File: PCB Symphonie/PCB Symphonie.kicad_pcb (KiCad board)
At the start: 2 copper layers, 81 parts, among them J1 Neopixel Clavier, J2 Neopixel Indicateur batterie, J3 Bornier Alim Ampli, J4 Bornier Signal ampli, Q1 2N3905, Q2 2N3905, Q3 2N3905, Q4 2N3905, SW0 SW_Push, SW1 SW_Push, SW10 SW_Push, SW11 SW_Push, SW12 SW_Push, SW13 SW_Push, SW14 SW_Push, SW15 SW_Push, SW16 SW_Push, SW17 SW_Push, SW18 SW_Push, SW19 SW_Push, SW2 SW_Push, SW20 SW_Push, SW21 SW_Push, SW22 SW_Push, SW23 SW_Push, SW24 SW_Push, SW3 SW_Push, SW4 SW_Push, SW5 SW_Push, SW6 SW_Push, SW7 SW_Push, SW8 SW_Push, SW9 SW_Push, U1 LM317_TO-220, U2 LM317_TO-220, U3 LM317_TO-220, U4 LM317_TO-220

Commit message: MAJ Pin changement shematique verifier empreintes
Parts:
- removed D15, D16, D17, D18, D19, D20, D21, D22, D23, D24: 1N4148, Diode_THT:D_DO-35_SOD27_P7.62mm_Horizontal
- removed SW0, SW1, SW10, SW11, SW12, SW13, SW14, SW15, SW16, SW17, SW18, SW19, SW2, SW20, SW21, SW22, SW23, SW24, SW3, SW4, SW5, SW6, SW7, SW8, SW9: SW_Push, Button_Switch_THT:SW_Tactile_Straight_KSA0Axx1LFTR
- added C1: C_Polarized_Small, Capacitor_SMD:CP_Elec_5x5.4, F.Cu at (89.5, 40.6)
- added C10: C, Capacitor_THT:CP_Radial_D8.0mm_P3.80mm, F.Cu at (76.8, 22.9)
- added C11: C, Capacitor_THT:CP_Radial_D8.0mm_P3.80mm, F.Cu at (76.8, 32.4)
- added C12: C_Polarized_Small, Capacitor_SMD:CP_Elec_5x5.4, F.Cu at (89.5, 61.2)
- added C2: C, Capacitor_THT:CP_Radial_D8.0mm_P3.80mm, F.Cu at (47.5, 22.9)
- added C3: C, Capacitor_THT:CP_Radial_D8.0mm_P3.80mm, F.Cu at (47.5, 32.4)
- added C4: C, Capacitor_THT:CP_Radial_D8.0mm_P3.80mm, F.Cu at (57.3, 22.9)
- added C5: C, Capacitor_THT:CP_Radial_D8.0mm_P3.80mm, F.Cu at (57.3, 32.4)
- added C6: C_Polarized_Small, Capacitor_SMD:CP_Elec_5x5.4, F.Cu at (89.5, 47.5)
- added C7: C, Capacitor_THT:CP_Radial_D8.0mm_P3.80mm, F.Cu at (67.0, 22.9)
- added C8: C, Capacitor_THT:CP_Radial_D8.0mm_P3.80mm, F.Cu at (67.0, 32.4)
- added C9: C_Polarized_Small, Capacitor_SMD:CP_Elec_5x5.4, F.Cu at (89.5, 54.3)
- added D25: LED, LED_THT:LED_D3.0mm, F.Cu at (91.3, 78.7)
- added D26: LED, LED_THT:LED_D3.0mm, F.Cu at (91.3, 84.2)
- added D27: LED, LED_THT:LED_D3.0mm, F.Cu at (91.3, 89.7)
- added J10: Bornier alim neopix, Connector:JWT_A3963_1x02_P3.96mm_Vertical, F.Cu at (68.9, 89.5)
- added J5: Conn_01x15_Pin, Connector_PinHeader_2.54mm:PinHeader_1x15_P2.54mm_Vertical, F.Cu at (78.0, 39.5)
- added J6: Conn_01x15_Pin, Connector_PinHeader_2.54mm:PinHeader_1x15_P2.54mm_Vertical, F.Cu at (82.7, 39.5)
- added J7: Conn_01x12_Pin, Connector_PinSocket_2.54mm:PinSocket_1x12_P2.54mm_Vertical, F.Cu at (87.3, 66.9)
- added J9: Bornier alim neopix, Connector:JWT_A3963_1x02_P3.96mm_Vertical, F.Cu at (68.9, 79.9)
- added R18: R, Resistor_THT:R_Axial_DIN0204_L3.6mm_D1.6mm_P7.62mm_Horizontal, F.Cu at (45.9, 92.3)
- added R19: R, Resistor_THT:R_Axial_DIN0204_L3.6mm_D1.6mm_P7.62mm_Horizontal, F.Cu at (45.9, 95.5)
- added SW25: SW_Push_Open, Connector_USB:USB_C_Plug_JAE_DX07P024AJ1, F.Cu at (99.1, 40.1)
- J1: value Neopixel Clavier -> Neopix batt; footprint Connector_PinHeader_2.54mm:PinHeader_1x04_P2.54mm_Vertical -> Connector:JWT_A3963_1x02_P3.96mm_Vertical
- J2: value Neopixel Indicateur batterie -> Neopix piano; footprint Connector_PinHeader_2.54mm:PinHeader_1x04_P2.54mm_Vertical -> Connector:JWT_A3963_1x02_P3.96mm_Vertical
- Q1, Q2, Q3, Q4: footprint Package_TO_SOT_THT:TO-3P-3_Horizontal_TabDown -> Package_TO_SOT_THT:TO-3P-3_Vertical
- RV1: footprint Potentiometer_SMD:Potentiometer_ACP_CA6-VSMD_Vertical -> Potentiometer_THT:Potentiometer_ACP_CA9-H5_Horizontal
- U1, U2, U3, U4: footprint Package_TO_SOT_SMD:SOT-89-3_Handsoldering -> Package_TO_SOT_THT:TO-3P-3_Vertical
- moved U1 68.1 mm to (30.5, 49.1)
- moved U2 68.0 mm to (30.5, 55.9)
- moved U3 67.8 mm to (30.5, 62.7)
- moved U4 67.7 mm to (30.5, 69.5)
- moved D28 66.3 mm to (56.6, 92.2)
- moved Q4 63.9 mm to (30.5, 42.3)
- moved D14 62.8 mm to (56.6, 88.7)
- moved D9 62.8 mm to (56.6, 70.9)
- moved D10 62.8 mm to (56.6, 74.5)
- moved D11 62.8 mm to (56.6, 78.0)
- moved D12 62.8 mm to (56.6, 81.6)
- moved D13 62.8 mm to (56.6, 85.1)
- moved Q1 62.5 mm to (30.5, 21.9)
- moved Q3 57.9 mm to (30.5, 35.5)
- moved Q2 57.4 mm to (30.5, 28.7)
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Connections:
- D0 pad 2: Net-(D0-A) -> unconnected-(D0-A-Pad2)
- D1 pad 2: Net-(D1-A) -> unconnected-(D1-A-Pad2)
- D10 pad 2: Net-(D10-A) -> unconnected-(D10-A-Pad2)
- D11 pad 2: Net-(D11-A) -> unconnected-(D11-A-Pad2)
- D12 pad 2: Net-(D12-A) -> unconnected-(D12-A-Pad2)
- D13 pad 2: Net-(D13-A) -> unconnected-(D13-A-Pad2)
- D14 pad 2: Net-(D14-A) -> unconnected-(D14-A-Pad2)
- D2 pad 2: Net-(D2-A) -> unconnected-(D2-A-Pad2)
- D3 pad 2: Net-(D3-A) -> unconnected-(D3-A-Pad2)
- D4 pad 2: Net-(D4-A) -> unconnected-(D4-A-Pad2)
- D5 pad 2: Net-(D5-A) -> unconnected-(D5-A-Pad2)
- D6 pad 2: Net-(D6-A) -> unconnected-(D6-A-Pad2)
- D7 pad 2: Net-(D7-A) -> unconnected-(D7-A-Pad2)
- D8 pad 2: Net-(D8-A) -> unconnected-(D8-A-Pad2)
- D9 pad 2: Net-(D9-A) -> unconnected-(D9-A-Pad2)
- J1 pad 1: NEOPIX 1 -> ROW0
- J1 pad 2: GND MC -> Net-(J1-Pin_2)
- J2 pad 1: NEOPIX 2 -> ROW0
- J2 pad 2: GND MC -> Net-(J2-Pin_2)
- Q3 pad 3: 5V Alim -> Net-(J9-Pin_2)
- R10 pad 2: 5V Alim -> Net-(J9-Pin_2)
- U3 pad 2: 5V Alim -> Net-(J9-Pin_2)
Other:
- board outline added: 152 x 105 mm

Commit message: Modif shema, Alim fait par simon
Debut PCB
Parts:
- removed C1, C12, C6, C9: C_Polarized_Small, Capacitor_SMD:CP_Elec_5x5.4
- removed C10, C11, C2, C3, C4, C5, C7, C8: C, Capacitor_THT:CP_Radial_D8.0mm_P3.80mm
- removed D25, D27: LED, LED_THT:LED_D3.0mm
- removed D28: 1N4148, Diode_THT:D_DO-35_SOD27_P7.62mm_Horizontal
- removed J10, J9: Bornier alim neopix, Connector:JWT_A3963_1x02_P3.96mm_Vertical
- removed Q1, Q2, Q3, Q4: 2N3905, Package_TO_SOT_THT:TO-3P-3_Vertical
- removed R1, R10, R11, R12, R13, R14, R15, R16, R17, R2, R3, R4, R5, R6, R7, R8, R9: R, Resistor_THT:R_Axial_DIN0204_L3.6mm_D1.6mm_P7.62mm_Horizontal
- removed SW25: SW_Push_Open, Connector_USB:USB_C_Plug_JAE_DX07P024AJ1
- removed U1, U2, U3, U4: LM317_TO-220, Package_TO_SOT_THT:TO-3P-3_Vertical
- added J11: Conn_01x12_Pin, Connector_PinSocket_2.54mm:PinSocket_1x12_P2.54mm_Vertical, F.Cu at (161.1, 130.1)
- added J12: Neopix batt, Connector:JWT_A3963_1x02_P3.96mm_Vertical, F.Cu at (141.0, 73.1)
- added J13: Neopix batt, Connector:JWT_A3963_1x02_P3.96mm_Vertical, F.Cu at (142.2, 99.1)
- added J8: Neopix batt, Connector:JWT_A3963_1x02_P3.96mm_Vertical, F.Cu at (142.5, 86.1)
- J3: value Bornier Alim Ampli -> Alim ESP32
- moved R19 214.1 mm to (259.1, 75.4), turned to 180 degrees
- moved J1 214.0 mm to (274.2, 101.4), turned to 90 degrees
- moved R18 208.1 mm to (253.9, 97.4)
- moved J2 205.3 mm to (272.2, 78.9), turned to 90 degrees
- moved RV1 183.0 mm to (272.5, 40.0)
- moved J7 166.0 mm to (240.1, 132.0), turned to 90 degrees
- moved D26 148.5 mm to (232.7, 39.0)
- moved D11 142.9 mm to (195.9, 109.5), turned to -90 degrees
- moved D10 141.9 mm to (191.9, 117.1), turned to 90 degrees
- moved D9 139.3 mm to (187.9, 117.3), turned to 90 degrees
- moved D8 136.7 mm to (183.9, 117.1), turned to 90 degrees
- moved D7 134.5 mm to (180.0, 117.3), turned to 90 degrees
- moved D6 132.7 mm to (176.4, 117.3), turned to 90 degrees
- moved D5 131.1 mm to (172.9, 117.3), turned to 90 degrees
- moved D4 129.7 mm to (169.3, 117.3), turned to 90 degrees
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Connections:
- D0 pad 2: unconnected-(D0-A-Pad2) -> RC
- D1 pad 2: unconnected-(D1-A-Pad2) -> RC#
- D10 pad 2: unconnected-(D10-A-Pad2) -> RA#
- D11 pad 2: unconnected-(D11-A-Pad2) -> RB
- D12 pad 2: unconnected-(D12-A-Pad2) -> R_BT1
- D13 pad 2: unconnected-(D13-A-Pad2) -> R_BT2
- D14 pad 2: unconnected-(D14-A-Pad2) -> R_BT3
- D2 pad 2: unconnected-(D2-A-Pad2) -> RD
- D3 pad 2: unconnected-(D3-A-Pad2) -> RD#
- D4 pad 2: unconnected-(D4-A-Pad2) -> RE
- D5 pad 2: unconnected-(D5-A-Pad2) -> RF
- D6 pad 2: unconnected-(D6-A-Pad2) -> RF#
- D7 pad 2: unconnected-(D7-A-Pad2) -> RG
- D8 pad 2: unconnected-(D8-A-Pad2) -> RG#
- D9 pad 2: unconnected-(D9-A-Pad2) -> RA
- J3 pad 2: Net-(J3-Pin_2) -> 3v3
- J6 pad 10: A# -> CB
- J6 pad 11: A# -> CD
- J6 pad 12: COL3 -> CD#
- J6 pad 13: A -> CA#
- J6 pad 7: COL4 -> CA
- J7 pad 1: A -> CA#
- J7 pad 10: A -> CA
- J7 pad 11: A# -> CA#
- J7 pad 12: A# -> CB
- J7 pad 2: A# -> CB
- J7 pad 3: A# -> CD
- J7 pad 4: COL3 -> CD#
- J7 pad 5: COL4 -> CA
- J7 pad 6: A -> CA#
- J7 pad 7: A# -> CB
- J7 pad 8: COL3 -> CD
- J7 pad 9: COL4 -> CD#

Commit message: maj pcb
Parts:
- moved J6 20.8 mm to (188.2, 41.4)
- moved J5 15.2 mm to (205.7, 41.7)
- moved D0 7.84 mm to (156.0, 109.7), turned to -90 degrees
- moved D1 7.84 mm to (159.5, 109.7), turned to -90 degrees
- moved D2 7.83 mm to (162.9, 109.7), turned to -90 degrees
- moved D3 7.83 mm to (166.4, 109.7), turned to -90 degrees
- moved D4 7.65 mm to (170.0, 109.7), turned to -90 degrees
- moved D5 7.64 mm to (173.5, 109.7), turned to -90 degrees
- moved D6 7.64 mm to (177.0, 109.7), turned to -90 degrees
- moved D7 7.64 mm to (180.5, 109.7), turned to -90 degrees
- moved D9 7.62 mm to (188.0, 109.7), turned to -90 degrees
- moved D10 7.43 mm to (192.0, 109.7), turned to -90 degrees
- moved D8 7.43 mm to (184.0, 109.7), turned to -90 degrees
- moved D12 0.50 mm to (161.3, 90.0)
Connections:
- J5 pad 12: ROW3 -> unconnected-(J5-Pin_12-Pad12)
- J5 pad 6: ROW4 -> unconnected-(J5-Pin_6-Pad6)
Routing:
- net RB: track 0.00 -> 17.7 mm
- net RC: track 0.00 -> 16.3 mm
- net RA#: track 0.00 -> 15.0 mm
- net RC#: track 0.00 -> 14.4 mm
- net RA: track 0.00 -> 14.4 mm
- net RD: track 0.00 -> 14.1 mm
- net RG#: track 0.00 -> 13.8 mm
- net RD#: track 0.00 -> 13.7 mm
- net RG: track 0.00 -> 13.4 mm
- net RE: track 0.00 -> 13.2 mm
- net RF#: track 0.00 -> 13.0 mm
- net RF: track 0.00 -> 12.8 mm
- net R_BT2: track 0.00 -> 12.2 mm
- net R_BT3: track 0.00 -> 11.6 mm
- net R_BT1: track 0.00 -> 11.2 mm

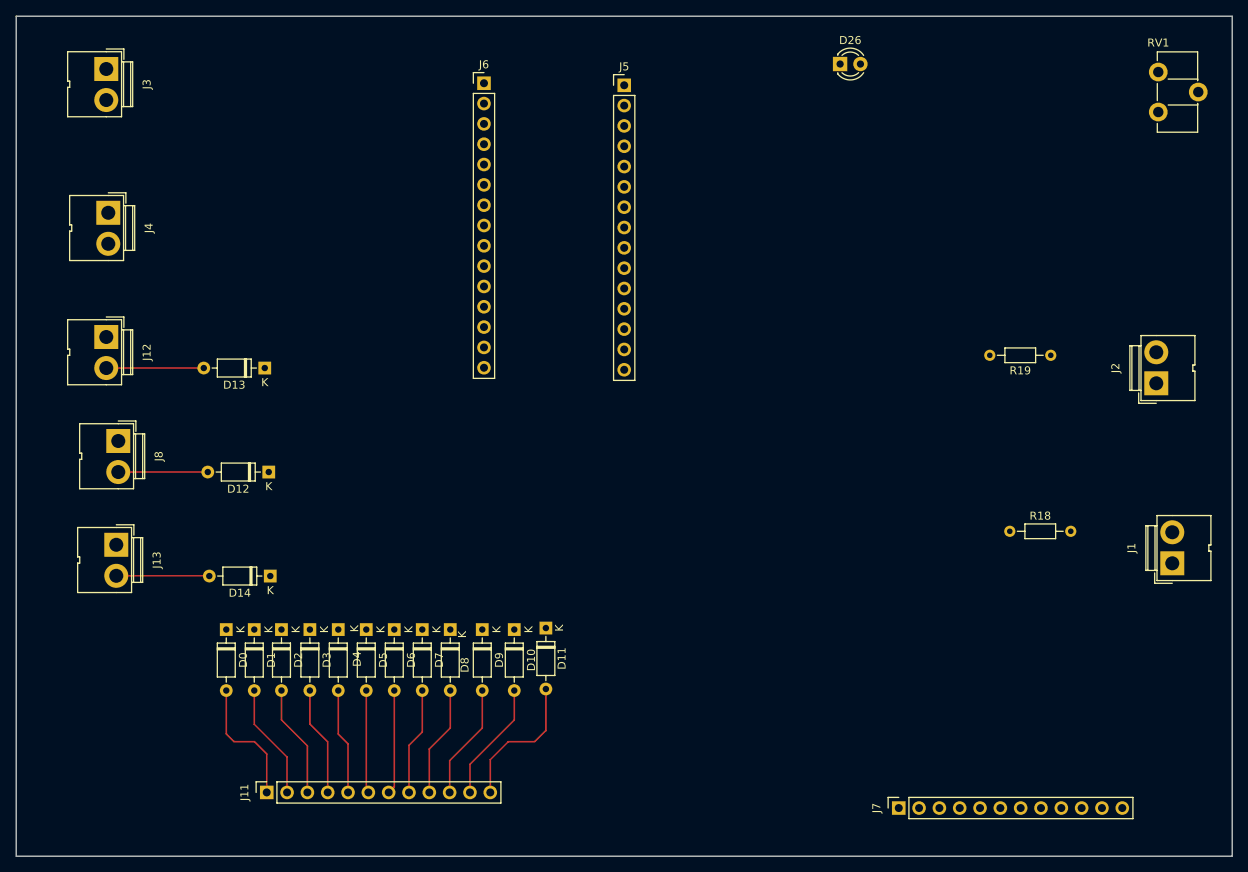
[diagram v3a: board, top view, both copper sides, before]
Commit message: Routage bien avancer ajout mode auto
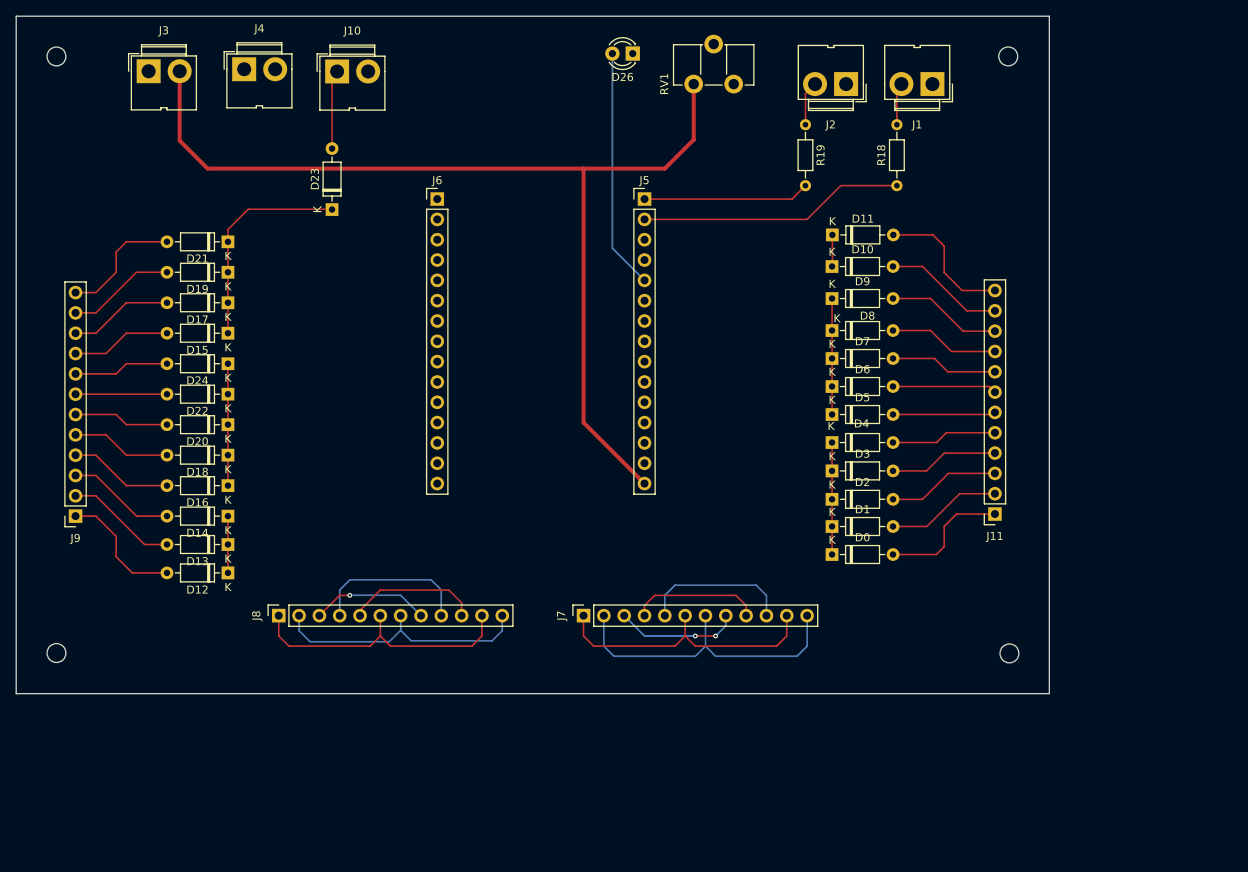
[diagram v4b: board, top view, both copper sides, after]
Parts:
- removed J12, J13: Neopix batt, Connector:JWT_A3963_1x02_P3.96mm_Vertical
- added D15: 1N4148, Diode_THT:D_DO-35_SOD27_P7.62mm_Horizontal, F.Cu at (156.2, 72.7)
- added D16: 1N4148, Diode_THT:D_DO-35_SOD27_P7.62mm_Horizontal, F.Cu at (156.2, 91.7)
- added D17: 1N4148, Diode_THT:D_DO-35_SOD27_P7.62mm_Horizontal, F.Cu at (156.2, 68.8)
- added D18: 1N4148, Diode_THT:D_DO-35_SOD27_P7.62mm_Horizontal, F.Cu at (156.2, 87.9)
- added D19: 1N4148, Diode_THT:D_DO-35_SOD27_P7.62mm_Horizontal, F.Cu at (156.2, 65.0)
- added D20: 1N4148, Diode_THT:D_DO-35_SOD27_P7.62mm_Horizontal, F.Cu at (156.2, 84.1)
- added D21: 1N4148, Diode_THT:D_DO-35_SOD27_P7.62mm_Horizontal, F.Cu at (156.2, 61.2)
- added D22: 1N4148, Diode_THT:D_DO-35_SOD27_P7.62mm_Horizontal, F.Cu at (156.2, 80.3)
- added D23: 1N4148, Diode_THT:D_DO-35_SOD27_P7.62mm_Horizontal, F.Cu at (169.2, 57.2)
- added D24: 1N4148, Diode_THT:D_DO-35_SOD27_P7.62mm_Horizontal, F.Cu at (156.2, 76.5)
- added J10: BTN, Connector:JWT_A3963_1x02_P3.96mm_Vertical, F.Cu at (169.9, 39.9)
- added J9: Ligne Octave 2, Connector_PinSocket_2.54mm:PinSocket_1x12_P2.54mm_Vertical, F.Cu at (137.2, 95.5)
- J11: value Conn_01x12_Pin -> Ligne Octave 1
- J7: value Conn_01x12_Pin -> Colonne Octave 1
- J8: value Neopix batt -> Colonne Octave 2; footprint Connector:JWT_A3963_1x02_P3.96mm_Vertical -> Connector_PinSocket_2.54mm:PinSocket_1x12_P2.54mm_Vertical
- moved J11 97.4 mm to (252.1, 95.2), turned to 180 degrees
- moved D0 76.3 mm to (231.7, 100.3), turned to 0 degrees
- moved D1 73.4 mm to (231.7, 96.8), turned to 0 degrees
- moved D2 70.7 mm to (231.7, 93.4), turned to 0 degrees
- moved D3 68.2 mm to (231.7, 89.9), turned to 0 degrees
- moved J1 67.0 mm to (244.3, 41.5), turned to 180 degrees
- moved D4 66.0 mm to (231.7, 86.3), turned to 0 degrees
- moved D5 64.1 mm to (231.7, 82.8), turned to 0 degrees
- moved D6 62.6 mm to (231.7, 79.3), turned to 0 degrees
- moved D7 61.4 mm to (231.7, 75.8), turned to 0 degrees
- moved D11 60.8 mm to (231.8, 60.4), turned to 0 degrees
- moved D8 60.6 mm to (231.7, 72.3), turned to 0 degrees
- moved D10 60.3 mm to (231.7, 64.3), turned to 0 degrees
- moved D9 60.2 mm to (231.7, 68.3), turned to 0 degrees
- moved RV1 58.1 mm to (214.4, 41.5), turned to 90 degrees
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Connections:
- D10 pad 1: ROW0 -> ROW2
- D11 pad 1: ROW0 -> ROW2
- D12 pad 1: ROW0 -> ROW2
- D12 pad 2: R_BT1 -> RC2
- D13 pad 1: ROW0 -> ROW2
- D13 pad 2: R_BT2 -> RC#2
- D14 pad 1: ROW0 -> ROW2
- D14 pad 2: R_BT3 -> RD2
- D26 pad 1: ROW0 -> Earth
- D5 pad 1: ROW0 -> ROW1
- D6 pad 1: ROW0 -> ROW1
- D7 pad 1: ROW0 -> ROW1
- D8 pad 1: ROW0 -> ROW1
- D9 pad 1: ROW0 -> ROW1
- J1 pad 1: ROW0 -> Earth
- J2 pad 1: ROW0 -> Earth
- J3 pad 1: ROW0 -> Earth
- J3 pad 2: 3v3 -> +3.3V
- J4 pad 1: ROW0 -> Earth
- J5 pad 14: ROW0 -> Earth
- J5 pad 15: 3v3 -> +3.3V
- J5 pad 7: ROW0 -> ROW2
- J5 pad 9: ROW0 -> ROW1
- J6 pad 10: CB -> CA2
- J6 pad 11: CD -> CA#2
- J6 pad 12: CD# -> CB2
- J6 pad 14: ROW0 -> Earth
- J7 pad 12: CB -> CA2
- J7 pad 2: CB -> CA2
- J7 pad 3: CD -> CA#2
- J7 pad 4: CD# -> CB2
- J7 pad 6: CA# -> unconnected-(J7-Pin_6-Pad6)
- J7 pad 7: CB -> CA2
- J7 pad 8: CD -> CA#2
- J7 pad 9: CD# -> CB2
- J8 pad 1: CD -> CA#2
- J8 pad 2: R_BT1 -> CB2
- RV1 pad 3: ROW0 -> Earth
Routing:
- net +3.3V: track 0.00 -> 125.4 mm
- net CA2: track 0.00 -> 55.6 mm
- net CA#: track 0.00 -> 55.3 mm
- net CA#2: track 0.00 -> 50.7 mm, vias 0 -> 2
- net CB2: track 0.00 -> 49.5 mm
- net CA: track 0.00 -> 33.6 mm, vias 0 -> 1
- net NEOPIX 2: track 0.00 -> 33.3 mm
- net LED BLE: track 0.00 -> 30.0 mm
- net ROW4: track 0.00 -> 27.0 mm
- net NEOPIX 1: track 0.00 -> 20.8 mm
- net RC2: track 0.00 -> 15.9 mm
- net RB2: track 0.00 -> 15.5 mm
- net ROW3: track 0.00 -> 15.2 mm
- net ROW1: track 0.00 -> 14.5 mm
- net ROW0: track 0.00 -> 14.0 mm
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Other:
- board size 152 x 105 mm -> 129.1 x 84.7 mm

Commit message: Fin cours 4mars
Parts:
- removed RV1: R_Potentiometer, Potentiometer_THT:Potentiometer_ACP_CA9-H5_Horizontal
- added D25: LED, LED_THT:LED_D3.0mm, F.Cu at (134.6, 53.8)
- added R1: R, Resistor_THT:R_Axial_DIN0204_L3.6mm_D1.6mm_P7.62mm_Horizontal, F.Cu at (141.0, 53.8)
- J1: value Neopix batt -> Neopix Batt; footprint Connector:JWT_A3963_1x02_P3.96mm_Vertical -> TerminalBlock:TerminalBlock_MaiXu_MX126-5.0-02P_1x02_P5.00mm
- J10, J2, J3: footprint Connector:JWT_A3963_1x02_P3.96mm_Vertical -> TerminalBlock:TerminalBlock_MaiXu_MX126-5.0-02P_1x02_P5.00mm
- J4: value Bornier Signal ampli -> Bornier Signal Ampli; footprint Connector:JWT_A3963_1x02_P3.96mm_Vertical -> TerminalBlock:TerminalBlock_MaiXu_MX126-5.0-02P_1x02_P5.00mm
- moved J3 62.3 mm to (208.6, 40.9)
- moved D26 15.5 mm to (222.2, 39.1)
- moved J4 5.22 mm to (153.2, 40.9), turned to 180 degrees
- moved J10 4.74 mm to (174.5, 40.9), turned to 180 degrees
- moved J2 3.88 mm to (229.7, 40.6), turned to 0 degrees
- moved J7 2.54 mm to (200.7, 105.4)
- moved J8 2.54 mm to (162.6, 105.4)
- moved D23 2.07 mm to (169.2, 55.1)
- moved J1 1.84 mm to (242.7, 40.6), turned to 0 degrees
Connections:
- J1 pad 1: Earth -> Net-(J1-Pin_1)
- J1 pad 2: Net-(J1-Pin_2) -> Earth
- J10 pad 1: R_BTN -> CA
- J10 pad 2: CA -> R_BTN
- J2 pad 1: Earth -> Net-(J2-Pin_1)
- J2 pad 2: Net-(J2-Pin_2) -> Earth
- J3 pad 1: Earth -> +3.3V
- J3 pad 2: +3.3V -> Earth
- J4 pad 1: Earth -> AMPLIFIER INPUT
- J4 pad 2: AMPLIFIER INPUT -> Earth
- J5 pad 11: unconnected-(J5-Pin_11-Pad11) -> ROW3
- J5 pad 6: unconnected-(J5-Pin_6-Pad6) -> ROW4
- J7 pad 1: CA# -> CB2
- J7 pad 10: CA -> CA#
- J7 pad 11: CA# -> CA#2
- J7 pad 12: CA2 -> CA#2
- J7 pad 2: CA2 -> CB2
- J7 pad 3: CA#2 -> CA2
- J7 pad 4: CB2 -> CA2
- J7 pad 5: CA -> CA2
- J7 pad 6: unconnected-(J7-Pin_6-Pad6) -> CA
- J7 pad 7: CA2 -> CA
- J7 pad 8: CA#2 -> CA#
- J7 pad 9: CB2 -> CA#
- J8 pad 10: CA2 -> CB2
- J8 pad 11: CA#2 -> CB2
- J8 pad 2: CB2 -> CA#2
- J8 pad 3: CA -> CA#2
- J8 pad 5: CA2 -> CA#
- J8 pad 6: unconnected-(J8-Pin_6-Pad6) -> CA
- J8 pad 7: CB2 -> CA
- J8 pad 8: CA -> CA2
- J8 pad 9: CA# -> CA2
- R18 pad 2: Net-(J1-Pin_2) -> Net-(J1-Pin_1)
- R19 pad 1: Net-(J2-Pin_2) -> Net-(J2-Pin_1)
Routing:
- net CA: track 33.6 -> 147.1 mm, vias 1 -> 0
- net ROW2: track 11.1 -> 106.5 mm, vias 0 -> 1
- net ROW3: track 15.2 -> 92.3 mm, vias 0 -> 1
- net CA#2: track 50.7 -> 104.5 mm, vias 2 -> 0
- net ROW4: track 27.0 -> 78.8 mm, vias 0 -> 1
- net AMPLIFIER INPUT: track 0.00 -> 48.6 mm, vias 0 -> 1
- net CA2: track 55.6 -> 83.1 mm
- net CA#: track 55.3 -> 82.5 mm
- net ROW0: track 14.0 -> 40.6 mm
- net ROW1: track 14.5 -> 38.1 mm
- net +3.3V: track 125.4 -> 112.4 mm
- net CB2: track 49.5 -> 40.6 mm
- net Net-(J1-Pin_1): track 0.00 -> 7.11 mm
- net Net-(J2-Pin_1): track 0.00 -> 6.48 mm
- net Net-(D25-K): track 0.00 -> 6.35 mm
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- added copper zone on B.Cu, net Earth
- added copper zone on F.Cu, net Earth
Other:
- board text added: "3V3"
- board text added: "BTN"
- board text added: "Colonne octave 1"
- board text added: "Colonne octave 2"
- board text added: "FA ESE 2025 KANE KANIA MARTIN"
- board text added: "Ligne Octave 1"
- board text added: "Ligne Octave 2"
- board text added: "NEOPIX BATTERIE"
- board text added: "NEOPIX PIANO"
- board text added: "Sortie signal"
